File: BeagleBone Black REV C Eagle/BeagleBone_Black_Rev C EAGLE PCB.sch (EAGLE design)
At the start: 379 parts, among them J1 68000-406HLF, P10 SCHA5B0200, P2 CTIJTAG, P3 87520-0010BLF, P4 UX60SC-MB-5ST(80), P5 LPJ0011BBNL, P6 10118241-001RLF, P8 SSHS-123-D-02-GT-LF, U10 TPD4S012, U11 TDA19988BHN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

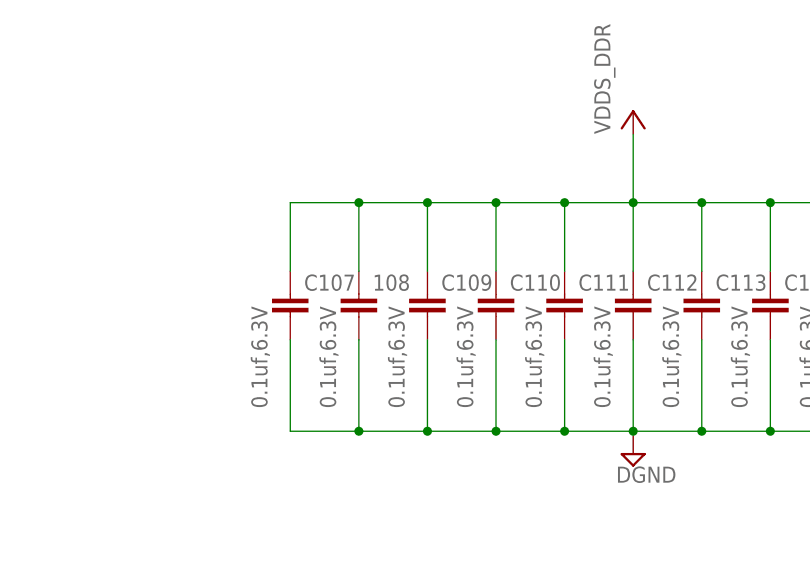
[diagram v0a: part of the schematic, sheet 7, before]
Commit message: import BeagleBone Black BOM
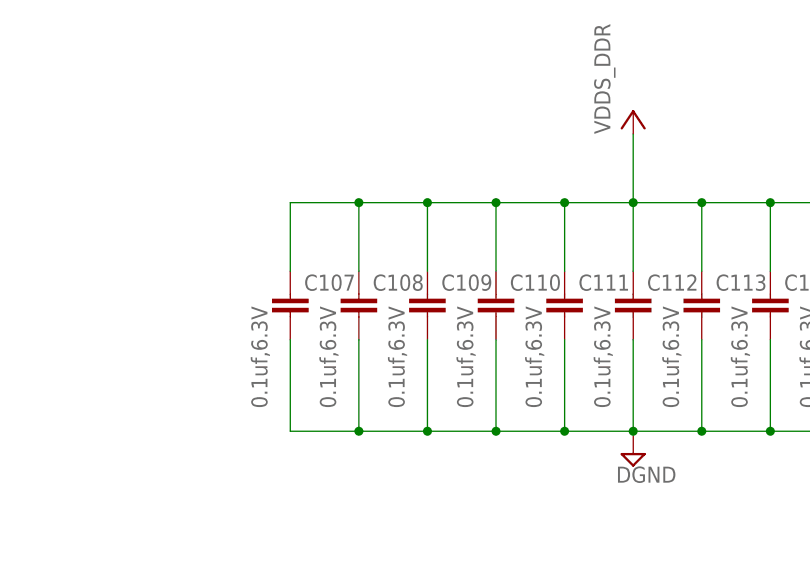
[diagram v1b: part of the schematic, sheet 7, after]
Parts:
- renumbered 108 to C108
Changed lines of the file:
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@@
 <?xml version="1.0" encoding="utf-8"?>
 <!DOCTYPE eagle SYSTEM "eagle.dtd">
-<eagle version="7.2.0">
+<eagle version="7.4.0">
 <drawing>
 <settings>
@@
 <part name="SUPPLY118" library="supply2" deviceset="GND" device="" value="DGND"/>
 <part name="C107" library="rcl" deviceset="C-EU" device="C0402"/>
-<part name="108" library="rcl" deviceset="C-EU" device="C0402"/>
+<part name="C108" library="rcl" deviceset="C-EU" device="C0402"/>
 <part name="C109" library="rcl" deviceset="C-EU" device="C0402"/>
 <part name="C110" library="rcl" deviceset="C-EU" device="C0402"/>
@@
 <instance part="SUPPLY118" gate="GND" x="182.88" y="355.6" rot="R270"/>
 <instance part="C107" gate="G$1" x="358.14" y="231.14"/>
-<instance part="108" gate="G$1" x="365.76" y="231.14"/>
+<instance part="C108" gate="G$1" x="365.76" y="231.14"/>
 <instance part="C109" gate="G$1" x="373.38" y="231.14"/>
 <instance part="C110" gate="G$1" x="381" y="231.14"/>
@@
 <wire x1="426.72" y1="215.9" x2="434.34" y2="215.9" width="0.1524" layer="91"/>
 <wire x1="434.34" y1="215.9" x2="434.34" y2="226.06" width="0.1524" layer="91"/>
-<pinref part="108" gate="G$1" pin="2"/>
+<pinref part="C108" gate="G$1" pin="2"/>
 <wire x1="365.76" y1="226.06" x2="365.76" y2="215.9" width="0.1524" layer="91"/>
 <pinref part="C109" gate="G$1" pin="2"/>
@@
 <pinref part="C109" gate="G$1" pin="1"/>
 <wire x1="373.38" y1="233.68" x2="373.38" y2="241.3" width="0.1524" layer="91"/>
-<pinref part="108" gate="G$1" pin="1"/>
+<pinref part="C108" gate="G$1" pin="1"/>
 <wire x1="365.76" y1="233.68" x2="365.76" y2="241.3" width="0.1524" layer="91"/>
 <junction x="365.76" y="241.3"/>
